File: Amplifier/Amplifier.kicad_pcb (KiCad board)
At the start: 2 copper layers, 55 x 52 mm, 43 parts, among them Q3 2N7002, U13 AD40xxBRMZ, U14 LP5907MFX-1.8, U16 LTC6268xS8, U2 LMP7721, U6 ADA4940-1xCP

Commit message: lots of layout changes.
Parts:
- removed R_DAMP1: 49.9, Resistor_SMD:R_0402_1005Metric
- added C9: 100nF, Capacitor_SMD:C_0805_2012Metric, F.Cu at (1.73, 1.00)
- added H1: FluidHole, MountingHole:MountingHole_2.1mm, F.Cu at (147.2, 68.5)
- added H2: FluidHole, MountingHole:MountingHole_2.1mm, F.Cu at (181.8, 48.5)
- added H3: FluidHole, MountingHole:MountingHole_2.1mm, F.Cu at (147.2, 48.5)
- added H4: FluidHole, MountingHole:MountingHole_2.1mm, F.Cu at (181.8, 68.5)
- added J7: Conn_01x14_MountingPin, Connector_FFC-FPC:Amphenol_F32R-1A7x1-11014_1x14-1MP_P0.5mm_Horizontal, F.Cu at (165.8, 83.0)
- J_POGO1: footprint footprints:PogoPin_SpringHeader_6Pin_Array -> footprints:PogoPin_Target_6Pin_Distributed
- moved R14 59.0 mm to (180.0, 76.9)
- moved R15 55.6 mm to (176.2, 79.4)
- moved Q3 46.7 mm to (179.4, 74.4)
- moved D82 45.4 mm to (176.3, 81.9)
- moved R30 45.0 mm to (168.3, 75.7), turned to -90 degrees
- moved R29 44.1 mm to (167.3, 75.7), turned to -90 degrees
- moved R28 43.7 mm to (166.3, 75.7), turned to -90 degrees
- moved R31 41.0 mm to (164.8, 75.7), turned to -90 degrees
- moved C41 40.4 mm to (162.0, 71.6), turned to 90 degrees
- moved U14 39.1 mm to (172.8, 71.2)
- moved U13 39.1 mm to (165.8, 70.7)
- moved R27 39.0 mm to (161.4, 73.3)
- moved C39 38.7 mm to (156.8, 82.7)
- moved C31 38.0 mm to (155.3, 76.2), turned to 180 degrees
- moved C35 37.7 mm to (158.9, 70.3), turned to 180 degrees
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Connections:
- J_POGO1 pad 4: /R_WEEP_LIM -> /WS_CIS
- J_POGO1 pad 5: /WS_CIS -> /R_WEEP_LIM
- R29 pad 1: /GDAC_SDI -> /GDAC_EN
- R30 pad 1: /GDAC_EN -> /GDAC_SDI
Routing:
- net +3V3: track 0.00 -> 32.3 mm, vias 0 -> 2
- net VDDA: track 29.7 -> 55.3 mm, vias 2 -> 5
- net />PORE_AMP: track 0.00 -> 24.8 mm, vias 0 -> 1
- net GND: track 0.00 -> 22.6 mm
- net VSSA: track 28.1 -> 48.9 mm, vias 3 -> 5
- net /Vbias: track 34.7 -> 53.3 mm
- net /Virtual_Ground: track 7.24 -> 25.4 mm
- net /R_WEEP_LIM: track 0.00 -> 18.2 mm, vias 0 -> 1
- net /SHIELD_AMP: track 18.2 -> 2.50 mm
- net /R_WEEP_PULL: track 0.00 -> 13.3 mm, vias 0 -> 2
- net +1V8: track 0.00 -> 11.8 mm
- net /GUARD: track 9.74 -> 19.3 mm, vias 11 -> 0
- net /GDAC_CLK: track 0.00 -> 6.71 mm
- net Net-(U13-IN+): track 0.00 -> 6.20 mm
- net /GDAC_SDI: track 0.00 -> 6.16 mm
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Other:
- board size 55 x 52 mm -> 57.1 x 56.5 mm

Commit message: commiting pcb changes
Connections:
- J7 pad 10: VSSA -> VDDA
- J7 pad 12: VDDA -> VSSA
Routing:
- net VDDA: track 55.3 -> 54.4 mm
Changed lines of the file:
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@@
 			(layers "F.Cu" "F.Mask" "F.Paste")
 			(roundrect_rratio 0.25)
-			(net "VSSA")
+			(net "VDDA")
 			(pinfunction "Pin_10_10")
 			(pintype "passive")
@@
 			(layers "F.Cu" "F.Mask" "F.Paste")
 			(roundrect_rratio 0.25)
-			(net "VDDA")
+			(net "VSSA")
 			(pinfunction "Pin_12_12")
 			(pintype "passive")
@@
 	)
 	(segment
-		(start 168.005 79.48509)
-		(end 168.76759 78.7225)
+		(start 162.523868 68.906932)
+		(end 162.1902 69.2406)
 		(width 0.2)
 		(layer "F.Cu")
@@
 	)
 	(segment
-		(start 162.523868 68.906932)
-		(end 162.1902 69.2406)
+		(start 167.005 79.256582)
+		(end 167.653009 78.608573)
 		(width 0.2)
 		(layer "F.Cu")
@@
 	)
 	(segment
-		(start 168.76759 78.7225)
-		(end 168.775 78.7225)
-		(width 0.2)
-		(layer "F.Cu")
-		(net "VDDA")
-	)
-	(segment
 		(start 156.505 76.315)
 		(end 156.005 76.315)
@@
 	)
 	(segment
+		(start 167.005 80.0675)
+		(end 167.005 79.256582)
+		(width 0.2)
+		(layer "F.Cu")
+		(net "VDDA")
+	)
+	(segment
 		(start 170.118434 61.178434)
 		(end 170.118434 63.0989)
@@
 	)
 	(segment
-		(start 168.005 80.0675)
-		(end 168.005 79.48509)
-		(width 0.2)
-		(layer "F.Cu")
-		(net "VDDA")
-	)
-	(segment
 		(start 170.1208 63.101266)
 		(end 170.1208 64.0484)
@@
 	)
 	(via
-		(at 168.775 78.7225)
+		(at 167.653009 78.608573)
 		(size 0.6)
 		(drill 0.3)
@@
 	)
 	(segment
-		(start 168.775 78.7225)
-		(end 168.044351 78.7225)
-		(width 0.2)
-		(layer "B.Cu")
-		(net "VDDA")
-	)
-	(segment
 		(start 157.005 75.815)
 		(end 159.243549 75.815)
@@
 	)
 	(segment
-		(start 168.044351 78.7225)
+		(start 167.653009 78.331158)
 		(end 162.1902 72.868349)
 		(width 0.2)
@@
 	)
 	(segment
+		(start 167.653009 78.608573)
+		(end 167.653009 78.331158)
+		(width 0.2)
+		(layer "B.Cu")
+		(net "VDDA")
+	)
+	(segment
 		(start 166.255 70.6925)
 		(end 167.855 70.6925)
@@
 	)
 	(segment
-		(start 166.955 79.417284)
-		(end 168.271332 78.100952)
+		(start 154.918434 64.8718)
+		(end 154.113 64.8718)
 		(width 0.2)
 		(layer "F.Cu")
@@
 	)
 	(segment
-		(start 154.918434 64.8718)
-		(end 154.113 64.8718)
+		(start 168.271332 78.100952)
+		(end 168.271332 79.218758)
 		(width 0.2)
 		(layer "F.Cu")
@@
 	)
 	(segment
-		(start 166.955 80.0175)
-		(end 166.955 79.417284)
-		(width 0.2)
-		(layer "F.Cu")
-		(net "VSSA")
-	)
-	(segment
 		(start 157.08 70.89)
 		(end 157.005 70.815)
@@
 	)
 	(segment
-		(start 167.005 80.0675)
-		(end 166.955 80.0175)
+		(start 162.865 61.0725)
+		(end 162.353244 61.0725)
 		(width 0.2)
 		(layer "F.Cu")
@@
 	)
 	(segment
-		(start 162.865 61.0725)
-		(end 162.353244 61.0725)
+		(start 155.58 72.0525)
+		(end 155.58 70.3325)
 		(width 0.2)
 		(layer "F.Cu")
@@
 	)
 	(segment
-		(start 155.58 72.0525)
-		(end 155.58 70.3325)
+		(start 168.271332 79.218758)
+		(end 168.005 79.48509)
 		(width 0.2)
 		(layer "F.Cu")
@@
 	)
 	(segment
+		(start 168.005 79.48509)
+		(end 168.005 80.0675)
+		(width 0.2)
+		(layer "F.Cu")
+		(net "VSSA")
+	)
+	(segment
 		(start 156.5025 70.3125)
 		(end 156.005 70.3125)
@@
 	)
 	(segment
-		(start 167.855 74.5825)
-		(end 167.255 75.1825)
+		(start 168.905 74.5325)
+		(end 168.255 75.1825)
 		(width 0.2)
 		(layer "F.Cu")
-		(net "/GDAC_EN")
+		(net "/GDAC_SDI")
 	)
 	(segment
-		(start 167.855 71.6925)
-		(end 167.855 74.5825)
+		(start 168.655432 70.1925)
+		(end 168.905 70.442068)
 		(width 0.2)
 		(layer "F.Cu")
-		(net "/GDAC_EN")
+		(net "/GDAC_SDI")
 	)
 	(segment
-		(start 165.505 78.9525)
-		(end 165.505 80.0675)
+		(start 168.905 70.442068)
+		(end 168.905 74.5325)
 		(width 0.2)
 		(layer "F.Cu")
-		(net "Net-(J7-Pin_7)")
+		(net "/GDAC_SDI")
 	)
 	(segment
-		(start 168.255 76.2025)
-		(end 165.505 78.9525)
+		(start 167.855 70.1925)
+		(end 168.655432 70.1925)
 		(width 0.2)
 		(layer "F.Cu")
-		(net "Net-(J7-Pin_7)")
+		(net "/GDAC_SDI")
 	)
 	(segment
-		(start 168.905 74.5325)
-		(end 168.255 75.1825)
+		(start 165.505 78.9525)
+		(end 165.505 80.0675)
 		(width 0.2)
 		(layer "F.Cu")
-		(net "/GDAC_SDI")
+		(net "Net-(J7-Pin_7)")
 	)
 	(segment
-		(start 168.655432 70.1925)
-		(end 168.905 70.442068)
+		(start 168.255 76.2025)
+		(end 165.505 78.9525)
 		(width 0.2)
 		(layer "F.Cu")
-		(net "/GDAC_SDI")
+		(net "Net-(J7-Pin_7)")
 	)
 	(segment
-		(start 168.905 70.442068)
-		(end 168.905 74.5325)
+		(start 167.855 74.5825)
+		(end 167.255 75.1825)
 		(width 0.2)
 		(layer "F.Cu")
-		(net "/GDAC_SDI")
+		(net "/GDAC_EN")
 	)
 	(segment
-		(start 167.855 70.1925)
-		(end 168.655432 70.1925)
+		(start 167.855 71.6925)
+		(end 167.855 74.5825)
 		(width 0.2)
 		(layer "F.Cu")
-		(net "/GDAC_SDI")
+		(net "/GDAC_EN")
 	)
 	(segment

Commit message: updated board, and worked to improve the project, added .agents which might be a mistake, along with the board updates
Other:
- board size 57.1 x 56.5 mm -> 55 x 52 mm
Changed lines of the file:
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@@
 	)
 	(gr_line
-		(start 149.5 84.48)
-		(end 158.5 84.48)
-		(stroke
-			(width 0.2)
-			(type default)
-		)
-		(layer "Edge.Cuts")
-	)
-	(gr_line
-		(start 158.5 81.9892)
-		(end 158.5 84.47)
-		(stroke
-			(width 0.2)
-			(type default)
-		)
-		(layer "Edge.Cuts")
-	)
-	(gr_line
-		(start 158.5 81.99)
-		(end 170.5 81.99)
-		(stroke
-			(width 0.2)
-			(type default)
-		)
-		(layer "Edge.Cuts")
-	)
-	(gr_line
-		(start 170.5 81.994244)
-		(end 170.5 84.475044)
-		(stroke
-			(width 0.2)
-			(type default)
-		)
-		(layer "Edge.Cuts")
-	)
-	(gr_line
-		(start 170.5 84.475044)
+		(start 149.5 84.475044)
+		(end 157.75 84.475044)
+		(stroke
+			(width 0.2)
+			(type default)
+		)
+		(layer "Edge.Cuts")
+	)
+	(gr_line
+		(start 157.75 81.475044)
+		(end 157.75 84.475044)
+		(stroke
+			(width 0.2)
+			(type default)
+		)
+		(layer "Edge.Cuts")
+	)
+	(gr_line
+		(start 157.75 81.475044)
+		(end 171.25 81.475044)
+		(stroke
+			(width 0.2)
+			(type default)
+		)
+		(layer "Edge.Cuts")
+	)
+	(gr_line
+		(start 171.25 81.475044)
+		(end 171.25 84.475044)
+		(stroke
+			(width 0.2)
+			(type default)
+		)
+		(layer "Edge.Cuts")
+	)
+	(gr_line
+		(start 171.25 84.475044)
 		(end 179.5 84.475044)
 		(stroke
@@
 	)
 	(gr_line
-		(start 185.06 30.415044)
-		(end 194.06 30.415044)
-		(stroke
-			(width 0.2)
-			(type default)
-		)
-		(layer "Edge.Cuts")
-	)
-	(gr_line
 		(start 189.5 58.494244)
 		(end 189.5154 58.101949)
@@
 		(stroke
 			(width 0.2)
-			(type default)
-		)
-		(layer "Edge.Cuts")
-	)
-	(gr_line
-		(start 194.06 30.415044)
-		(end 194.06 27.934244)
-		(stroke
-			(width 0.2)

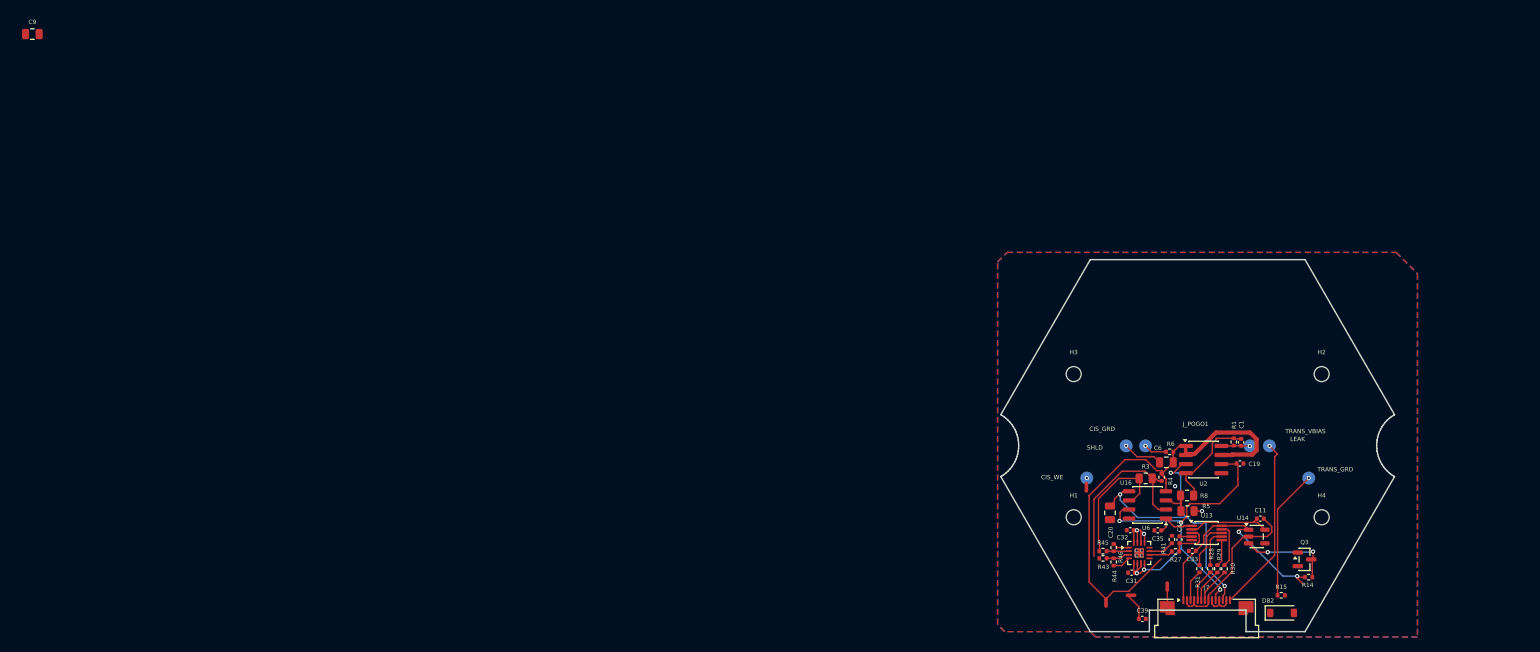
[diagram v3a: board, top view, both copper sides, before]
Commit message: chore: prepare repository and documentation for open-source release
- Removed internal .agents scaffolding and updated .gitignore
- Added CONTRIBUTING.md with CAD, PCB, firmware, and PR guidelines
- Added CODE_OF_CONDUCT.md (Contributor Covenant v2.1)
- Added SECURITY.md with hardware safety and vulnerability disclosure policies
- Added CITATION.cff for academic and scientific publications
- Added Pump_firmware/README.md for STM32G431 subsystem
- Expanded BOM.md with mechanical, fluidic, PCB, and active electronics
- Updated README.md test badges, architecture, and documentation index
- Cleared hardcoded absolute developer paths in export_manager.py and KiCad files
- Fixed formatting in install.sh and metadata in package.json
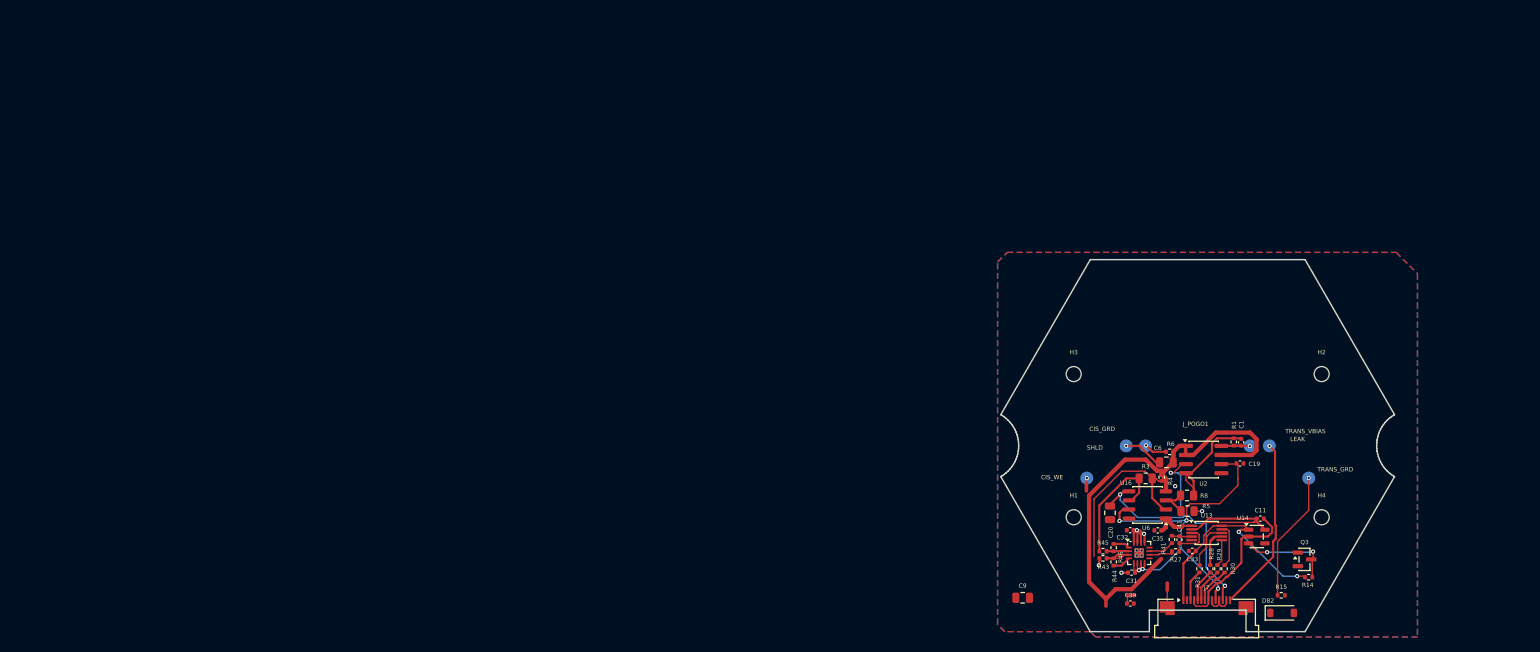
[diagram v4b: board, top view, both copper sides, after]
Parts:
- moved C9 159.2 mm to (140.1, 79.8)
- moved C39 2.72 mm to (155.1, 80.5)
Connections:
- net /Signal_AMP renamed /Signal_Return
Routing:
- net +1V8: track 11.8 -> 22.2 mm
- net /GDAC_SDO: track 5.30 -> 9.59 mm
- net /WS_CIS: track 3.99 -> 8.01 mm
- net VSSA: track 48.4 -> 52.4 mm
- net Net-(C1-Pad1): track 14.4 -> 17.8 mm
- net Net-(U6A--IN): track 3.33 -> 6.65 mm
- net Net-(U6A-+IN): track 3.12 -> 6.24 mm
- net Net-(C39-Pad1): track 3.96 -> 1.18 mm
- net GNDA: track 10.9 -> 12.9 mm, vias 3 -> 5
- net GND: track 22.6 -> 21.2 mm
- net Net-(U13-IN-): track 1.71 -> 2.80 mm
- net /Signal_Return: track 18.3 -> 17.4 mm
- net /CE_GNDA: track 0.00 -> 0.82 mm
- net +3V3: track 32.3 -> 33.1 mm
- net VDDA: track 54.4 -> 55.0 mm

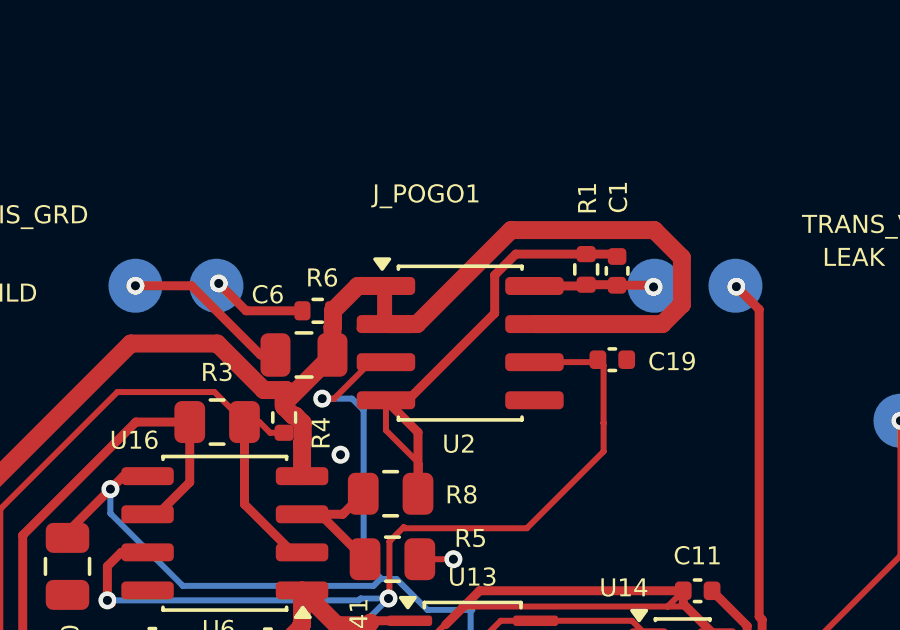
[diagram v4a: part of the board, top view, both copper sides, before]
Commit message: Configure 2-Layer PTFE Substrate, 3D Guarding & Rigid Anvil
Co-authored-by: google-labs-jules[bot] <161369871+google-labs-jules[bot]@users.noreply.github.com>
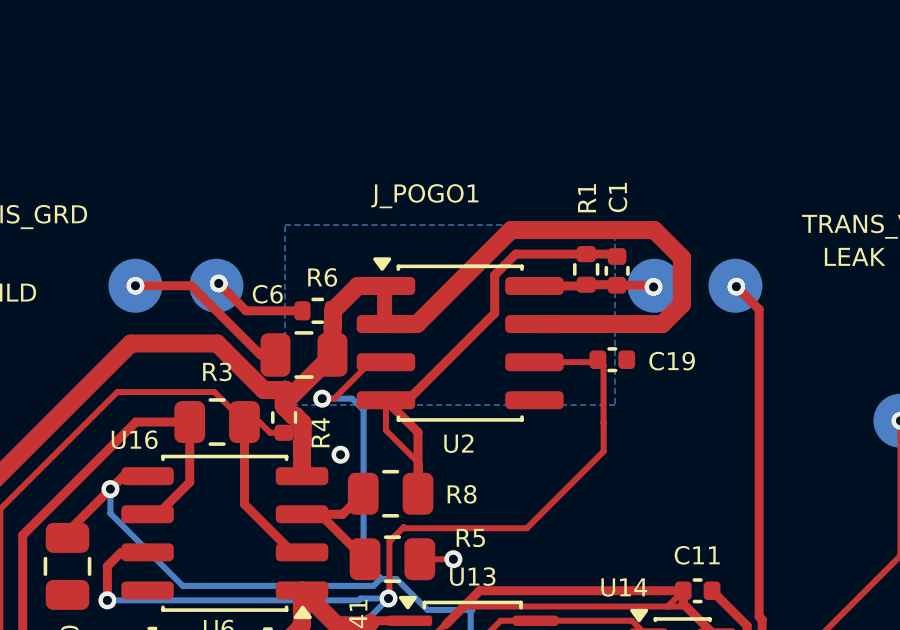
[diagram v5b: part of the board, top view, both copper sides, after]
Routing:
- added copper zone on B.Cu, net /GUARD
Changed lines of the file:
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@@
 				(type "core")
 				(color "PTFE natural")
-				(thickness 0.71)
-				(material "PTFE")
+				(thickness 1.5)
+				(material "Rogers RO3003 / PTFE")
 				(epsilon_r 2.1)
 				(loss_tangent 0.0002)
@@
 	)
 	(embedded_fonts no)
+	(gr_poly
+		(pts
+			(xy 159.0 56.0) (xy 171.0 56.0) (xy 171.0 63.0) (xy 159.0 63.0)
+		)
+		(stroke
+			(width 0.1)
+			(type solid)
+		)
+		(fill yes)
+		(layer "F.Mask")
+	)
+	(gr_poly
+		(pts
+			(xy 159.0 56.0) (xy 171.0 56.0) (xy 171.0 63.0) (xy 159.0 63.0)
+		)
+		(stroke
+			(width 0.1)
+			(type solid)
+		)
+		(fill yes)
+		(layer "B.Mask")
+	)
+	(zone
+		(keepout
+			(tracks allowed)
+			(vias allowed)
+			(pads allowed)
+			(copperpour not_allowed)
+			(footprints allowed)
+		)
+		(layers "B.Cu")
+		(hatch edge 0.5)
+		(polygon
+			(pts
+				(xy 159.0 56.0) (xy 171.0 56.0) (xy 171.0 63.0) (xy 159.0 63.0)
+			)
+		)
+	)
+	(zone
+		(net "/GUARD")
+		(layers "B.Cu")
+		(hatch edge 0.5)
+		(connect_pads
+			(clearance 0.15)
+		)
+		(min_thickness 0.15)
+		(polygon
+			(pts
+				(xy 159.5 56.5) (xy 170.5 56.5) (xy 170.5 62.5) (xy 159.5 62.5)
+			)
+		)
+	)
 )

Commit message: lots of refinements.
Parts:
- removed J_POGO1: PogoPin_SpringHeader_6Pin_Array, footprints:PogoPin_Target_6Pin_Distributed
- removed NT5: NetTie_2, NetTie:NetTie-2_SMD_Pad0.5mm
- added C14: 100nF, Capacitor_SMD:C_0805_2012Metric, F.Cu at (4.63, 12.7)
- added C3: 15pF, Capacitor_SMD:C_0402_1005Metric, F.Cu at (8.29, 12.2)
- added C34: 100nF, Capacitor_SMD:C_0402_1005Metric, F.Cu at (8.29, 14.2)
- added FB1: HZ0402A152R-10, Inductor_SMD:L_0402_1005Metric, F.Cu at (0.95, 5.64)
- added FB2: HZ0402A152R-10, Inductor_SMD:L_0402_1005Metric, F.Cu at (0.95, 7.63)
- added J_POGO2: PogoPin_SpringHeader_12Pin_Distributed, footprints:PogoPin_SpringHeader_12Pin_Distributed, F.Cu at (13.1, 2.08)
- added NT6: NetTie_2, NetTie:NetTie-2_SMD_Pad0.5mm, F.Cu at (3.66, 15.0)
- added R10: 100k, Resistor_SMD:R_0402_1005Metric, F.Cu at (0.95, 11.6)
- added R32: 49.9, Resistor_SMD:R_0402_1005Metric, F.Cu at (0.95, 13.6)
- added R33: 49.9, Resistor_SMD:R_0402_1005Metric, F.Cu at (0.95, 15.6)
- added R9: 1K, Resistor_SMD:R_0402_1005Metric, F.Cu at (0.95, 9.62)
- added U5: OPA192IDR, footprints:SOIC-8_3.9x4.9mm_P1.27mm, F.Cu at (6.63, 8.01)
- R1: value 1M -> 1G
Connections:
- C11 pad 2: GND -> GNDA
- C33 pad 1: +3V3 -> +3.3VA
- J7 pad 2: GND -> /GND
- J7 pad 4: GND -> Net-(J7-Pin_4)
- J7 pad 8: GND -> /GND
- U13 pad 10: +3V3 -> +3.3VA
- U14 pad 1: +3V3 -> Net-(U14-IN)
- U14 pad 2: GND -> GNDA
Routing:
- net GND: track 21.2 -> 0.00 mm
- net GNDA: track 12.9 -> 34.1 mm

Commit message: there's issues with the constrictic iterposer mating pad showing up
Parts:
- removed NT6: NetTie_2, NetTie:NetTie-2_SMD_Pad0.5mm

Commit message: adding new symbols
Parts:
- added C40: 100nF, Capacitor_SMD:C_0402_1005Metric, F.Cu at (208.6, 76.7)
- added C42: 100nF, Capacitor_SMD:C_0402_1005Metric, F.Cu at (208.6, 78.7)
- added J_PAD1: Concentric_Interposer_Mating_Pad, footprints:Concentric_Interposer_Mating_Pad, B.Cu at (204.6, 78.2)
- added J_POGO1: PogoPin_SpringHeader_6Pin_Cis, footprints:PogoPin_SpringHeader_6Pin_Cis, B.Cu at (164.5, 43.5)
- added U17: ADG1219BRMZ, footprints:MSOP-8_3x3mm_P0.65mm, F.Cu at (205.8, 73.4)
- J_POGO2: value PogoPin_SpringHeader_12Pin_Distributed -> PogoPin_SpringHeader_6Pin_Trans; footprint footprints:PogoPin_SpringHeader_12Pin_Distributed -> footprints:PogoPin_SpringHeader_6Pin_Trans; moved to B.Cu
- U5: value OPA192IDR -> OPA2192IDR
- moved C14 206.3 mm to (204.4, 64.3)
- moved C3 206.3 mm to (208.1, 63.8)
- moved C34 206.3 mm to (208.1, 65.8)
- moved U5 206.3 mm to (206.4, 59.6)
- moved FB1 206.3 mm to (200.7, 57.2)
- moved FB2 206.3 mm to (200.7, 59.2)
- moved R10 206.3 mm to (200.7, 63.2)
- moved R32 206.3 mm to (200.7, 65.2)
- moved R33 206.3 mm to (200.7, 67.2)
- moved R9 206.3 mm to (200.7, 61.2)
- moved J_POGO2 167.4 mm to (164.5, 73.5)
- moved J7 1.57 mm to (164.6, 81.9)
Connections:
- C3 pad 1: Net-(U5-~) -> Net-(U5A-~)
- C9 pad 1: /Signal_Return -> /Route1_OUT
- J_POGO2 pad 3: />PORE_AMP -> /GUARD_WIDE
- J_POGO2 pad 4: GNDA -> /WS_CIS_WIDE
- R10 pad 1: Net-(U5-~) -> Net-(U5A-~)
- R3 pad 1: /Signal_Return -> /Route1_OUT
- R32 pad 1: Net-(U5-~) -> Net-(U5A-~)
- R32 pad 2: /Signal_Return -> /Route2_OUT
- U16 pad 6: /Signal_Return -> /Route1_OUT
- U5 pad 1: unconnected-(U5-NC-Pad1) -> Net-(U5A-~)
- U5 pad 5: unconnected-(U5-NC-Pad5) -> /Vbias
- U5 pad 6: Net-(U5-~) -> /GUARD_WIDE
- U5 pad 7: VDDA -> /GUARD_WIDE
- U5 pad 8: unconnected-(U5-NC-Pad8) -> VDDA
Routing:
- net /SHIELD_AMP: track 2.50 -> 27.1 mm, vias 0 -> 1
- net />PORE_AMP: track 24.6 -> 0.00 mm, vias 1 -> 0
- net /GUARD: track 19.7 -> 34.8 mm
- net GNDA: track 34.1 -> 37.7 mm
- net /GUARD_WIDE: track 0.00 -> 1.55 mm
